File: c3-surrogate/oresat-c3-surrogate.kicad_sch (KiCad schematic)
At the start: 74 parts, among them J1 J-SAMTEC-TFM-120-X1-XXX-D-RA, J2 Conn_01x04, J3 1900468, J4 1995499, Q1 PMV45EN, Q3 NTR4101P, Q4 NTR4101P, Q5 DMP3050LVT-7, SW2 EG1218, SW3 OS203011MV9QS1, SW4 EG1218, U1 MAX892LEUA+T, U2 LTC4412xS6, U4 LTC4412xS6, U5 TS5A21366, U6 Trinket-M0

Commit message: More polishing, along with library cleanup
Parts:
- J3: footprint N/A -> (none)
- PCB3: renamed from U6; footprint Adafruit-Trinket-M0:Trinket-M0 -> oresat-pcbs:Adafruit-Trinket
- U1: footprint U-Maxim-MAX892LEUA+T-power-switch:MAX892LEUA+T -> oresat-ics:LINEAR-MSOP-8-AND-MAXIM-UMAX-8-21-0036; symbol oresat-passives:MAX892LEUA+T -> oresat-ics:MAX892LEUA+T
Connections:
- no-connect marks 14 -> 16
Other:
- moved on the sheet: R4, TP3, TP4

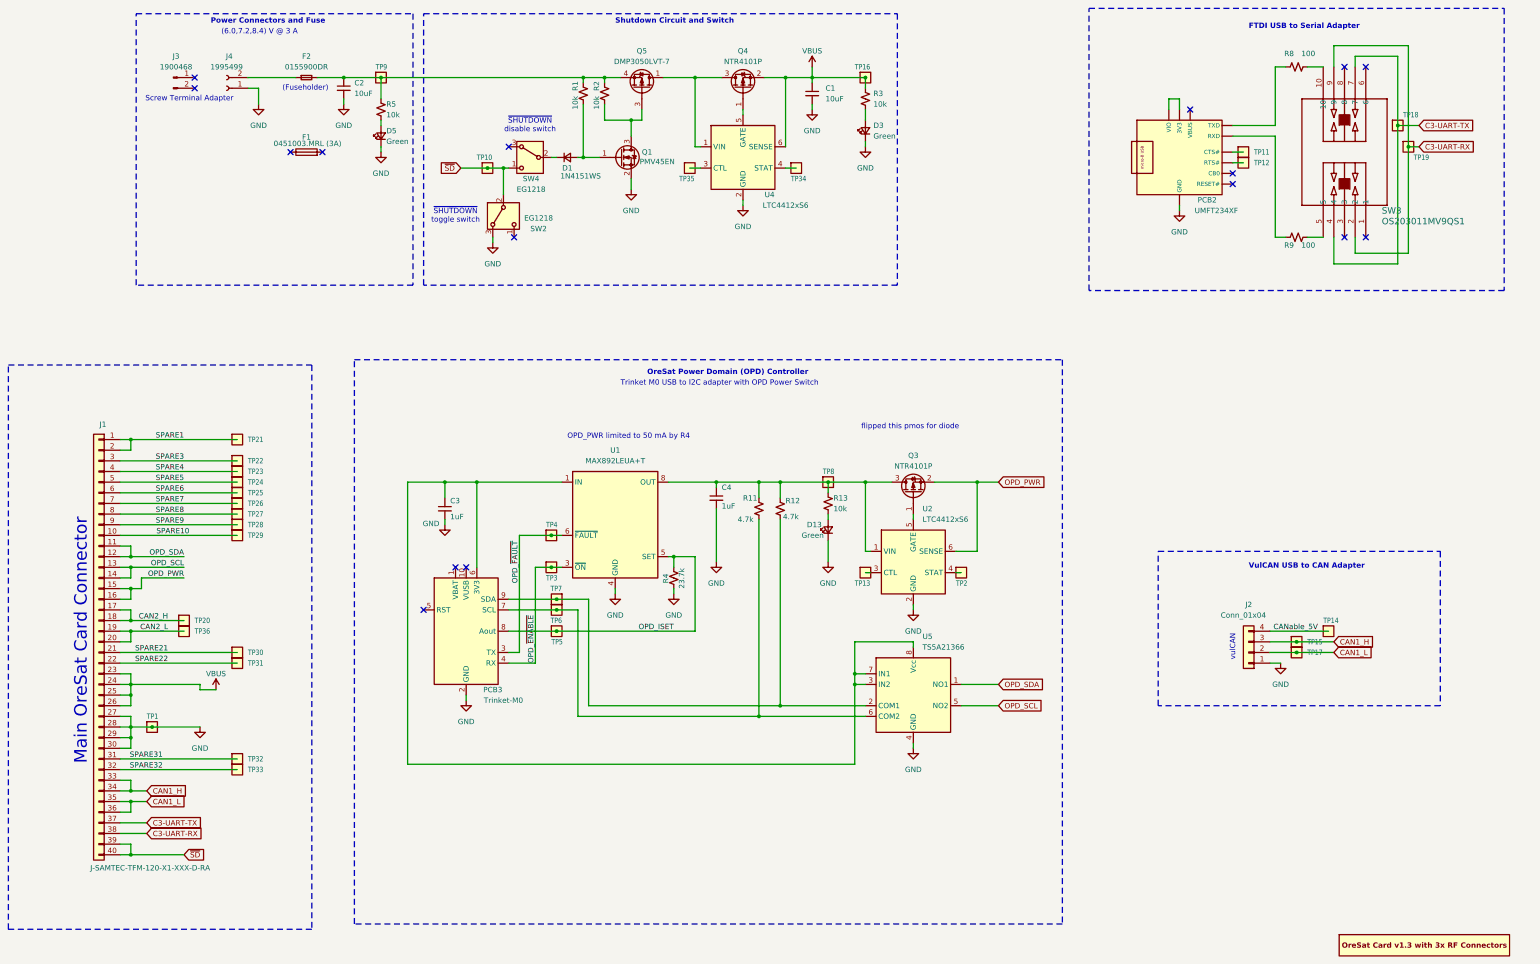
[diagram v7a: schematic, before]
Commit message: Updated KiCad version and fixed used libraries and paths.
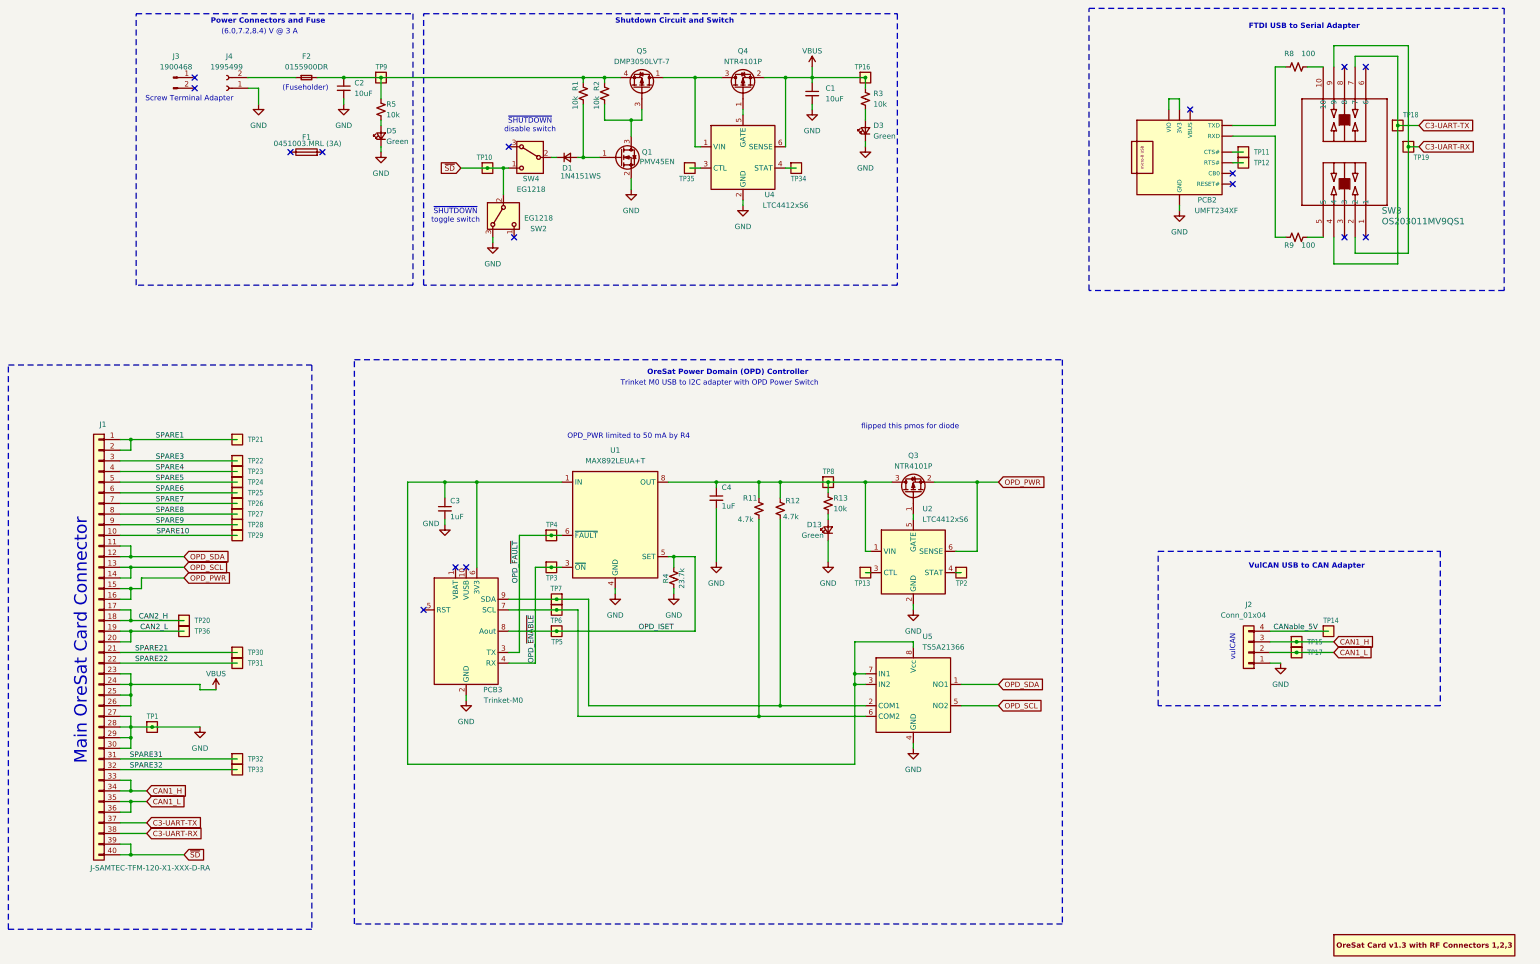
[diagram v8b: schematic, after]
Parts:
- Q1: symbol Device:Q_NMOS_GSD -> Transistor_FET:Q_NMOS_GSD
